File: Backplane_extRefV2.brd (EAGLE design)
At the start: 72.5 x 64.9 mm, 15 parts, among them J1 TFM-125-02-XXX-D-WT, U1 TLE2426CD

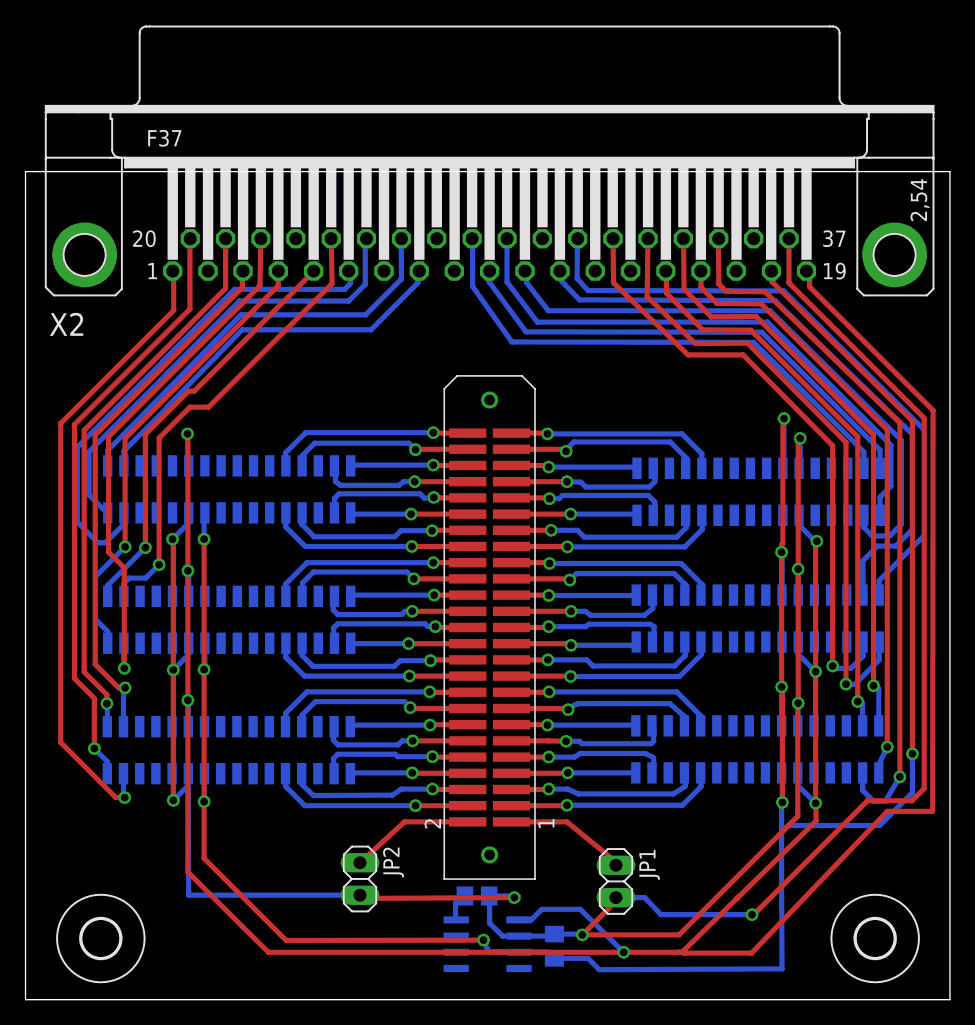
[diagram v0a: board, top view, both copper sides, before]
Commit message: minor updates to routing. Added DC-DC voltage converter/isolator to backplaneV2 & 24ch brd
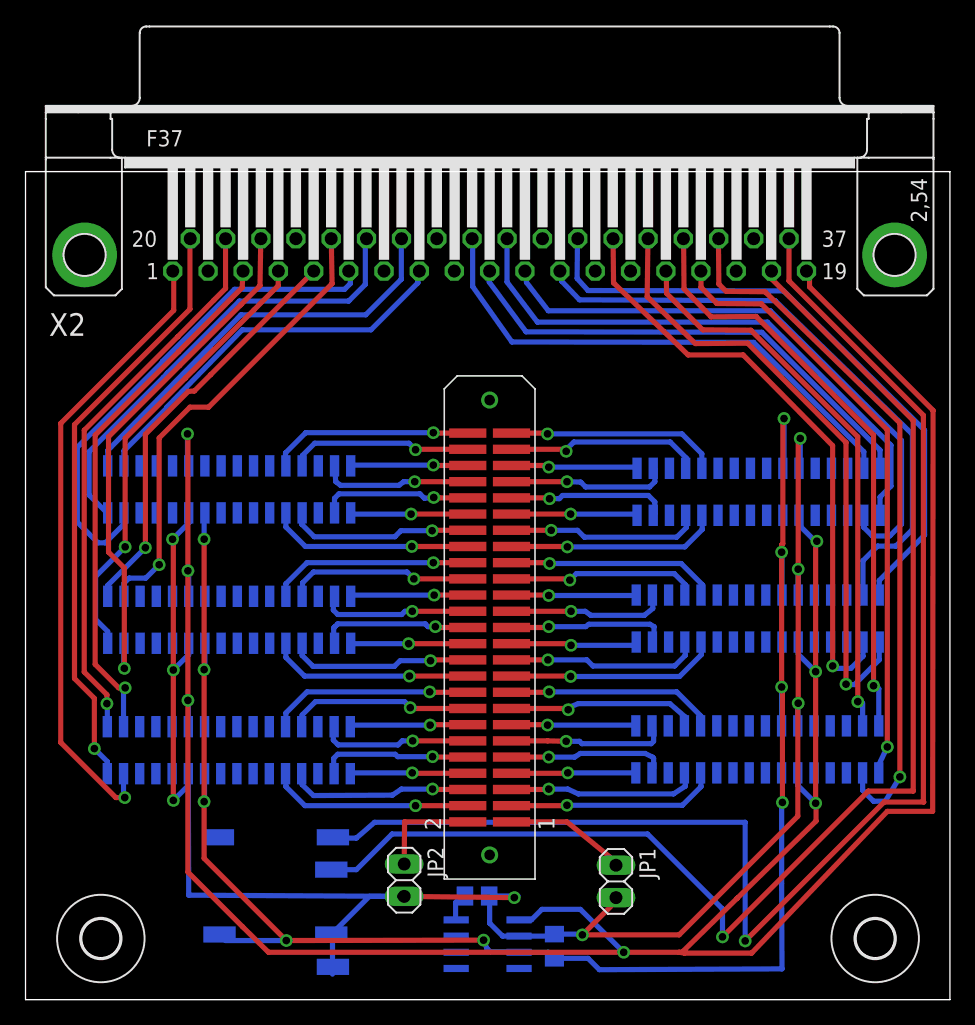
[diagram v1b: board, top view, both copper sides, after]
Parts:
- added U$9: R1Z-1205, tuckerLib:R1Z-1205
- moved JP2 3.46 mm to (29.7, 9.37)
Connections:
- new net +VIN: U$9.2, X2.18
- new net -VIN: U$9.1, X2.37
- new net NC2: U$9.10
- net GND: now also U$9.4, U$9.5; no longer X2.37
- net VCC: now also U$9.7; no longer X2.18
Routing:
- net -VIN: track 0.00 -> 109.2 mm, vias 0 -> 1
- net +VIN: track 0.00 -> 101.5 mm, vias 0 -> 1
- net GND: track 212.0 -> 146.0 mm
- net VCC: track 191.2 -> 139.6 mm
- net G2: track 9.69 -> 8.26 mm
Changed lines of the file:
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@@
 </element>
 <element name="JP1" library="pinhead" package="1X02" value="" x="46.355" y="9.271" rot="R270"/>
-<element name="JP2" library="pinhead" package="1X02" value="" x="26.289" y="9.4615" rot="R270"/>
+<element name="JP2" library="pinhead" package="1X02" value="" x="29.74975" y="9.36625" rot="R270"/>
 <element name="U$1" library="holes" package="3,0" value="" x="66.675" y="4.79425"/>
 <element name="U$2" library="holes" package="3,0" value="" x="5.969" y="4.79425"/>
@@
 <attribute name="OC_FARNELL" value="1931219" x="48.006" y="37.973" size="1.778" layer="28" rot="MR0" display="off"/>
 </element>
+<element name="U$9" library="tuckerLib" package="R1Z-1205" value="R1Z-1205" x="18.95475" y="7.65175" rot="MR270"/>
 </elements>
 <signals>
@@
 <wire x1="12.827" y1="16.79575" x2="12.827" y2="16.5735" width="0.4064" layer="16"/>
 <wire x1="12.827" y1="16.5735" x2="12.85875" y2="8.1915" width="0.4064" layer="16"/>
-<wire x1="12.85875" y1="8.1915" x2="26.289" y2="8.1915" width="0.4064" layer="16"/>
+<wire x1="12.85875" y1="8.1915" x2="29.74975" y2="8.09625" width="0.4064" layer="16"/>
 <wire x1="38.75405" y1="4.98475" x2="37.465" y2="4.98475" width="0.4064" layer="16"/>
 <wire x1="37.465" y1="4.98475" x2="36.449" y2="6.00075" width="0.4064" layer="16"/>
@@
 <wire x1="46.355" y1="8.001" x2="46.355" y2="7.71525" width="0.4064" layer="1"/>
 <wire x1="46.355" y1="7.71525" x2="43.71975" y2="5.08" width="0.4064" layer="1"/>
-<contactref element="X2" pad="37"/>
-<wire x1="59.9186" y1="59.65825" x2="59.9186" y2="56.19115" width="0.4064" layer="1"/>
-<wire x1="59.9186" y1="56.19115" x2="70.51675" y2="45.593" width="0.4064" layer="1"/>
-<wire x1="70.51675" y1="45.593" x2="70.51675" y2="16.54175" width="0.4064" layer="1"/>
-<wire x1="57.023" y1="6.6675" x2="49.87925" y2="6.6675" width="0.4064" layer="16"/>
-<wire x1="49.87925" y1="6.6675" x2="48.60925" y2="8.001" width="0.4064" layer="16"/>
-<wire x1="48.60925" y1="8.001" x2="46.355" y2="8.001" width="0.4064" layer="16"/>
 <wire x1="36.41475" y1="8.128" x2="38.6715" y2="8.128" width="0.4064" layer="16"/>
 <wire x1="38.6715" y1="8.128" x2="38.38575" y2="8.001" width="0.4064" layer="16"/>
 <via x="38.38575" y="8.001" extent="1-16" drill="0.6" shape="square"/>
-<wire x1="38.38575" y1="8.001" x2="26.543" y2="7.9375" width="0.4064" layer="1"/>
-<wire x1="26.543" y1="7.9375" x2="26.289" y2="8.1915" width="0.4064" layer="1"/>
-<via x="57.023" y="6.6675" extent="1-16" drill="0.6" shape="square"/>
-<wire x1="57.023" y1="6.6675" x2="57.15" y2="6.6675" width="0.4064" layer="1"/>
-<wire x1="57.15" y1="6.6675" x2="66.07175" y2="15.58925" width="0.4064" layer="1"/>
-<wire x1="66.07175" y1="15.58925" x2="69.56425" y2="15.58925" width="0.4064" layer="1"/>
-<wire x1="69.56425" y1="15.58925" x2="70.51675" y2="16.54175" width="0.4064" layer="1"/>
+<wire x1="38.38575" y1="8.001" x2="29.49575" y2="8.09625" width="0.4064" layer="1"/>
+<wire x1="29.49575" y1="8.09625" x2="29.74975" y2="8.09625" width="0.4064" layer="1"/>
+<contactref element="U$9" pad="4"/>
+<contactref element="U$9" pad="5"/>
+<wire x1="24.03475" y1="5.11175" x2="24.13" y2="5.11175" width="0.4064" layer="16"/>
+<wire x1="24.13" y1="5.11175" x2="24.13" y2="2.00025" width="0.4064" layer="16"/>
+<via x="29.49575" y="8.09625" extent="1-16" drill="0.6" shape="square"/>
+<wire x1="29.49575" y1="8.09625" x2="27.01925" y2="8.09625" width="0.4064" layer="16"/>
+<wire x1="27.01925" y1="8.09625" x2="24.03475" y2="5.11175" width="0.4064" layer="16"/>
+<wire x1="24.13" y1="2.00025" x2="24.16175" y2="2.57175" width="0" layer="19" extent="16-16"/>
 </signal>
 <signal name="O21">
@@
 <wire x1="45.05325" y1="2.3495" x2="59.3725" y2="2.413" width="0.4064" layer="16"/>
 <wire x1="59.3725" y1="2.413" x2="59.34075" y2="9.0805" width="0.4064" layer="16"/>
-<wire x1="59.34075" y1="9.0805" x2="59.34075" y2="13.11275" width="0.4064" layer="16"/>
-<wire x1="59.34075" y1="13.11275" x2="59.34075" y2="15.39875" width="0.4064" layer="16"/>
+<wire x1="59.34075" y1="9.0805" x2="59.34075" y2="15.39875" width="0.4064" layer="16"/>
 <wire x1="59.34075" y1="15.39875" x2="59.40425" y2="15.46225" width="0.4064" layer="16"/>
 <via x="59.40425" y="15.46225" extent="1-16" drill="0.6" shape="square"/>
 <wire x1="59.40425" y1="15.46225" x2="59.40425" y2="24.4475" width="0.4064" layer="1"/>
 <wire x1="59.40425" y1="24.4475" x2="59.34075" y2="24.511" width="0.4064" layer="1"/>
-<contactref element="X2" pad="18"/>
-<wire x1="58.547" y1="57.11825" x2="58.547" y2="56.3245" width="0.4064" layer="1"/>
-<wire x1="58.547" y1="56.3245" x2="69.596" y2="45.37075" width="0.4064" layer="1"/>
-<wire x1="69.596" y1="45.37075" x2="69.596" y2="19.27225" width="0.4064" layer="1"/>
-<via x="69.596" y="19.27225" extent="1-16" drill="0.6" shape="square"/>
-<wire x1="69.596" y1="19.27225" x2="69.596" y2="16.22425" width="0.4064" layer="16"/>
-<wire x1="69.596" y1="16.22425" x2="67.02425" y2="13.6525" width="0.4064" layer="16"/>
-<wire x1="67.02425" y1="13.6525" x2="59.8805" y2="13.6525" width="0.4064" layer="16"/>
-<wire x1="59.8805" y1="13.6525" x2="59.34075" y2="13.11275" width="0.4064" layer="16"/>
 <wire x1="14.097" y1="17.7165" x2="14.097" y2="15.5575" width="0.4064" layer="16"/>
 <wire x1="14.097" y1="15.5575" x2="14.06525" y2="15.52575" width="0.4064" layer="16"/>
@@
 <wire x1="14.06525" y1="15.52575" x2="14.06525" y2="11.08075" width="0.4064" layer="1"/>
 <wire x1="14.06525" y1="25.87625" x2="14.06525" y2="15.52575" width="0.4064" layer="1"/>
+<contactref element="U$9" pad="7"/>
+<via x="20.5105" y="4.6355" extent="1-16" drill="0.6" shape="square"/>
+<wire x1="20.5105" y1="4.6355" x2="15.748" y2="4.6355" width="0.4064" layer="16"/>
+<wire x1="15.748" y1="4.6355" x2="15.27175" y2="5.11175" width="0.4064" layer="16"/>
 </signal>
 <signal name="I23+">
@@
 <contactref element="JP2" pad="1"/>
 <wire x1="34.7345" y1="13.93825" x2="29.7815" y2="13.93825" width="0.4064" layer="1"/>
-<wire x1="29.7815" y1="13.93825" x2="26.289" y2="10.7315" width="0.4064" layer="1"/>
+<wire x1="29.7815" y1="13.93825" x2="29.74975" y2="10.63625" width="0.4064" layer="1"/>
 </signal>
 <signal name="G1">
@@
 <contactref element="X2" pad="13"/>
 </signal>
+<signal name="NC2">
+<contactref element="U$9" pad="10"/>
+</signal>
+<signal name="-VIN">
+<contactref element="U$9" pad="1"/>
+<contactref element="X2" pad="37"/>
+<wire x1="59.9186" y1="59.65825" x2="59.9186" y2="56.3499" width="0.4064" layer="1"/>
+<wire x1="59.9186" y1="56.3499" x2="70.45325" y2="45.81525" width="0.4064" layer="1"/>
+<wire x1="70.45325" y1="45.81525" x2="70.45325" y2="15.52575" width="0.4064" layer="1"/>
+<wire x1="70.45325" y1="15.52575" x2="70.485" y2="15.494" width="0.4064" layer="1"/>
+<wire x1="70.485" y1="15.494" x2="67.3735" y2="15.494" width="0.4064" layer="1"/>
+<wire x1="67.3735" y1="15.494" x2="56.48325" y2="4.60375" width="0.4064" layer="1"/>
+<via x="56.48325" y="4.60375" extent="1-16" drill="0.6" shape="square"/>
+<wire x1="56.48325" y1="4.60375" x2="56.48325" y2="13.9065" width="0.4064" layer="16"/>
+<wire x1="56.48325" y1="13.9065" x2="27.432" y2="13.9065" width="0.4064" layer="16"/>
+<wire x1="27.432" y1="13.9065" x2="26.00325" y2="12.66825" width="0.4064" layer="16"/>
+<wire x1="26.00325" y1="12.66825" x2="24.22525" y2="12.66825" width="0.4064" layer="16"/>
+<wire x1="24.22525" y1="12.66825" x2="24.16175" y2="12.73175" width="0.4064" layer="16"/>
+</signal>
+<signal name="+VIN">
+<contactref element="U$9" pad="2"/>
+<contactref element="X2" pad="18"/>
+<wire x1="58.547" y1="57.11825" x2="58.547" y2="56.515" width="0.4064" layer="1"/>
+<wire x1="58.547" y1="56.515" x2="69.6595" y2="45.4025" width="0.4064" layer="1"/>
+<wire x1="69.6595" y1="45.4025" x2="69.6595" y2="16.35125" width="0.4064" layer="1"/>
+<wire x1="69.6595" y1="16.35125" x2="66.13525" y2="16.35125" width="0.4064" layer="1"/>
+<wire x1="66.13525" y1="16.35125" x2="54.70525" y2="4.92125" width="0.4064" layer="1"/>
+<via x="54.70525" y="4.92125" extent="1-16" drill="0.6" shape="square"/>
+<wire x1="54.70525" y1="4.92125" x2="54.70525" y2="7.112" width="0.4064" layer="16"/>
+<wire x1="54.70525" y1="7.112" x2="48.8315" y2="12.98575" width="0.4064" layer="16"/>
+<wire x1="48.8315" y1="12.98575" x2="28.79725" y2="12.98575" width="0.4064" layer="16"/>
+<wire x1="28.79725" y1="12.98575" x2="26.00325" y2="10.19175" width="0.4064" layer="16"/>
+<wire x1="26.00325" y1="10.19175" x2="24.03475" y2="10.19175" width="0.4064" layer="16"/>
+</signal>
 </signals>
